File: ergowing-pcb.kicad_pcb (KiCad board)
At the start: 2 copper layers, 309.6 x 110.8 mm, 156 parts, among them J1 USB_mini_micro_B, K0:0 KEYSW, K0:1 KEYSW, K0:2 KEYSW, K0:3 KEYSW, K0:4 KEYSW, K10:0 KEYSW, K10:1 KEYSW, K10:2 KEYSW, K10:3 KEYSW, K10:4 KEYSW, K11:0 KEYSW, K11:1 KEYSW, K11:2 KEYSW, K11:3 KEYSW, K11:4 KEYSW, K12:0 KEYSW, K12:1 KEYSW, K12:2 KEYSW, K12:3 KEYSW, K12:4 KEYSW, K13:0 KEYSW, K13:1 KEYSW, K13:2 KEYSW, K13:3 KEYSW, K13:4 KEYSW, K1:0 KEYSW, K1:1 KEYSW, K1:2 KEYSW, K1:3 KEYSW, K1:4 KEYSW, K2:0 KEYSW, K2:1 KEYSW, K2:2 KEYSW, K2:3 KEYSW, K2:4 KEYSW, K3:0 KEYSW, K3:1 KEYSW, K3:2 KEYSW, K3:3 KEYSW, K3:4 KEYSW, K4:0 KEYSW, K4:1 KEYSW, K4:2 KEYSW, K4:3 KEYSW, K4:4 KEYSW, K5:0 KEYSW, K5:1 KEYSW, K5:2 KEYSW, K5:3 KEYSW, K5:4 KEYSW, K6:0 KEYSW, K6:1 KEYSW, K6:3 KEYSW, K7:0 KEYSW, K7:1 KEYSW, K7:3 KEYSW, K7:4 KEYSW, K8:0 KEYSW, K8:1 KEYSW, K8:2 KEYSW, K8:3 KEYSW, K8:4 KEYSW, K9:0 KEYSW, K9:1 KEYSW, K9:2 KEYSW, K9:3 KEYSW, K9:4 KEYSW, SW1 SW_PUSH, U1 ATMEGA32U4, X1 XTAL_GND

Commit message: Edge cuts lined up
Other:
- board size 309.6 x 110.8 mm -> 309.8 x 110.9 mm
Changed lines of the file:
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@@
     (links 522)
     (no_connects 0)
-    (area 46.80134 9.363663 355.995213 136.791998)
+    (area 42.554808 21.173406 352.858618 132.915581)
     (thickness 1.6)
-    (drawings 20)
+    (drawings 16)
     (tracks 1784)
     (zones 0)
@@
     (42 Eco1.User user)
     (43 Eco2.User user)
-    (44 Edge.Cuts user hide)
+    (44 Edge.Cuts user)
     (45 Margin user)
     (46 B.CrtYd user)
@@
   (gr_line (start 42.815024 119.692888) (end 51.430988 21.223407) (layer Eco1.User) (width 0.1))
   (gr_line (start 183.806712 132.140235) (end 42.815024 119.692888) (layer Eco1.User) (width 0.1))
-  (gr_line (start 351.218732 119.944908) (end 211.806719 132.140236) (layer Edge.Cuts) (width 0.15))
-  (gr_line (start 344.111389 22.59822) (end 352.491387 118.428217) (layer Edge.Cuts) (width 0.15))
-  (gr_line (start 203.656716 33.480237) (end 342.594697 21.325566) (angle 90) (layer Edge.Cuts) (width 0.15))
-  (gr_arc (start 342.716712 22.720234) (end 342.594697 21.325566) (angle 90) (layer Edge.Cuts) (width 0.15))
-  (gr_arc (start 351.096713 118.550241) (end 352.491387 118.428217) (angle 90) (layer Edge.Cuts) (width 0.15))
-  (gr_line (start 183.806712 132.140235) (end 44.209696 119.814906) (angle 90) (layer Edge.Cuts) (width 0.15))
-  (gr_line (start 191.756716 33.480241) (end 52.828733 21.345561) (angle 90) (layer Edge.Cuts) (width 0.15))
-  (gr_line (start 51.312043 22.618219) (end 42.937044 118.298221) (angle 90) (layer Edge.Cuts) (width 0.15))
-  (gr_arc (start 44.331715 118.420236) (end 44.209696 119.814906) (angle 90) (layer Edge.Cuts) (width 0.15))
-  (gr_arc (start 52.706714 22.740234) (end 51.312043 22.618219) (angle 90) (layer Edge.Cuts) (width 0.15))
-  (gr_line (start 191.756716 33.480241) (end 203.656716 33.480237) (angle 90) (layer Edge.Cuts) (width 0.15))
-  (gr_line (start 183.806712 132.140235) (end 211.806719 132.140236) (angle 90) (layer Edge.Cuts) (width 0.15))
+  (gr_line (start 352.618833 119.820771) (end 211.806713 132.140235) (layer Edge.Cuts) (width 0.15))
+  (gr_line (start 352.618833 119.820771) (end 343.991114 21.223471) (layer Edge.Cuts) (width 0.15))
+  (gr_line (start 203.656715 33.500237) (end 343.991114 21.223471) (angle 90) (layer Edge.Cuts) (width 0.15))
+  (gr_line (start 183.806712 132.140235) (end 42.815024 119.692888) (angle 90) (layer Edge.Cuts) (width 0.15))
+  (gr_line (start 51.430988 21.223407) (end 191.754973 33.500165) (angle 90) (layer Edge.Cuts) (width 0.15))
+  (gr_line (start 42.815024 119.692888) (end 51.430988 21.223407) (angle 90) (layer Edge.Cuts) (width 0.15))
+  (gr_line (start 191.754973 33.500165) (end 203.656715 33.500237) (angle 90) (layer Edge.Cuts) (width 0.15))
+  (gr_line (start 183.806712 132.140235) (end 211.806713 132.140235) (angle 90) (layer Edge.Cuts) (width 0.15))
   (segment (start 204.506716 100.650233) (end 204.506714 100.620234) (width 0.25) (layer B.Cu) (net 1))
   (segment (start 204.506714 100.620234) (end 202.7206 98.834118) (width 0.25) (layer B.Cu) (net 1))

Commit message: Update#1
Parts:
- moved D10:3 118.7 mm to (278.1, 216.4)
- moved D11:0 118.7 mm to (292.1, 160.2)
- moved D13:1 118.7 mm to (336.0, 178.5)
- moved D4:3 118.7 mm to (141.8, 219.6)
- moved K10:4 118.7 mm to (279.3, 230.8)
- moved K11:0 118.7 mm to (291.6, 155.8)
- moved K8:3 118.7 mm to (240.5, 218.1)
- moved C2 118.7 mm to (211.9, 223.0)
- moved D5:1 118.7 mm to (163.7, 185.1)
- moved K12:1 118.7 mm to (312.2, 176.1)
- moved K2:0 118.7 mm to (109.6, 155.8)
- moved K2:3 118.7 mm to (104.7, 212.0)
- moved K6:1 118.7 mm to (182.4, 187.1)
- moved U1 118.7 mm to (200.7, 228.2)
- moved X1 118.7 mm to (208.5, 220.1)
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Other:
- board size 309.8 x 110.9 mm -> 140.8 x 12.3 mm

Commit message: Start re-aligning keyswitches
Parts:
- moved D0:0 86.0 mm to (64.6, 245.6), turned to 0 degrees
- moved K0:0 86.0 mm to (64.6, 241.2), turned to 5 degrees
- moved K0:1 67.2 mm to (64.6, 241.2), turned to 5 degrees
- moved D0:1 67.2 mm to (64.6, 245.6), turned to 0 degrees
- moved D0:2 48.5 mm to (64.6, 245.6), turned to 0 degrees
- moved K0:2 48.5 mm to (64.6, 241.2), turned to 5 degrees
- moved D0:3 29.9 mm to (64.6, 245.6), turned to 0 degrees
- moved K0:3 29.9 mm to (64.6, 241.2), turned to 5 degrees
- moved D13:4 13.8 mm to (344.2, 221.3), turned to 10 degrees
- moved K13:4 13.6 mm to (343.5, 216.9), turned to 5 degrees
- moved D13:3 13.3 mm to (341.0, 202.8), turned to 10 degrees
- moved K13:3 13.2 mm to (340.2, 198.4), turned to 5 degrees
- moved K13:0 13.0 mm to (330.4, 142.8), turned to 5 degrees
- moved D13:2 13.0 mm to (337.8, 184.2), turned to 10 degrees
- moved D13:0 13.0 mm to (331.3, 147.2), turned to 10 degrees
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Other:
- board outline removed

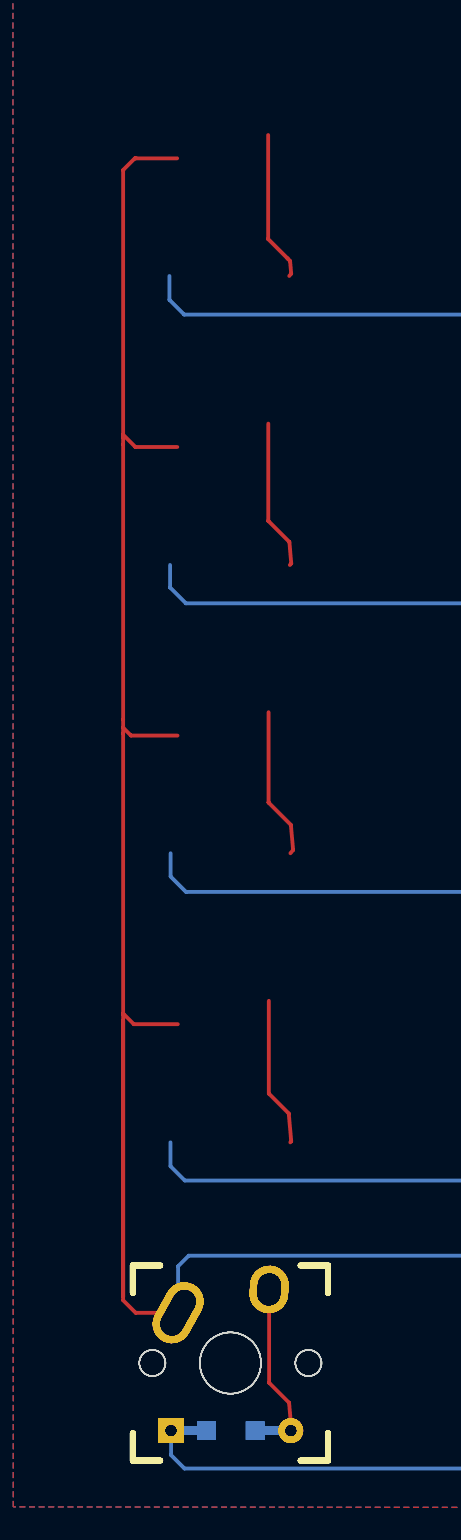
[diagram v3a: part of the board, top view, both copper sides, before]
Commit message: Col0 re-aligned *properly
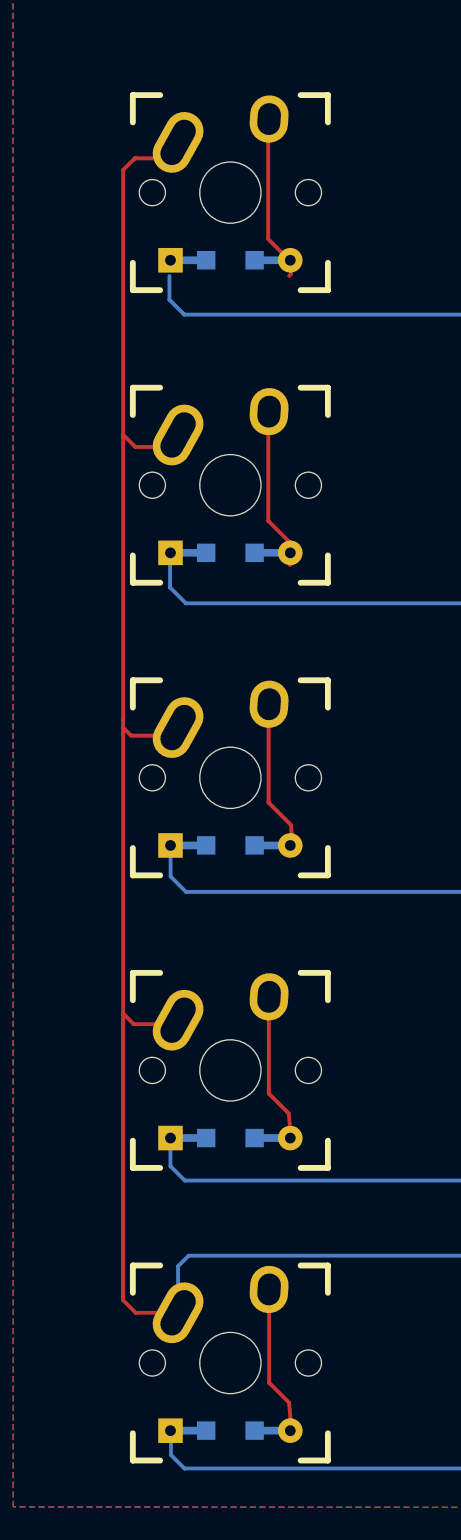
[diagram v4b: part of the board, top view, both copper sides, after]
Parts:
- moved D0:0 76.2 mm to (64.6, 169.4)
- moved K0:0 76.2 mm to (64.6, 165.0)
- moved D0:1 57.2 mm to (64.6, 188.5)
- moved K0:1 57.2 mm to (64.6, 184.1)
- moved D0:2 38.1 mm to (64.6, 207.5)
- moved K0:2 38.1 mm to (64.6, 203.1)
- moved D0:3 19.1 mm to (64.6, 226.6)
- moved K0:3 19.0 mm to (64.6, 222.2)
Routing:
- net (no net): track 0.00 -> 39.3 mm
- net row4: track 344.4 -> 318.8 mm
- net row0: track 364.4 -> 390.0 mm
- net Net-(D0:0-Pad2): track 9.82 -> 0.00 mm
- net Net-(D0:3-Pad2): track 9.78 -> 0.00 mm
- net Net-(D0:4-Pad2): track 9.75 -> 0.00 mm
- net Net-(D0:1-Pad2): track 9.81 -> 3.69 mm
- net Net-(D0:2-Pad2): track 9.86 -> 6.06 mm

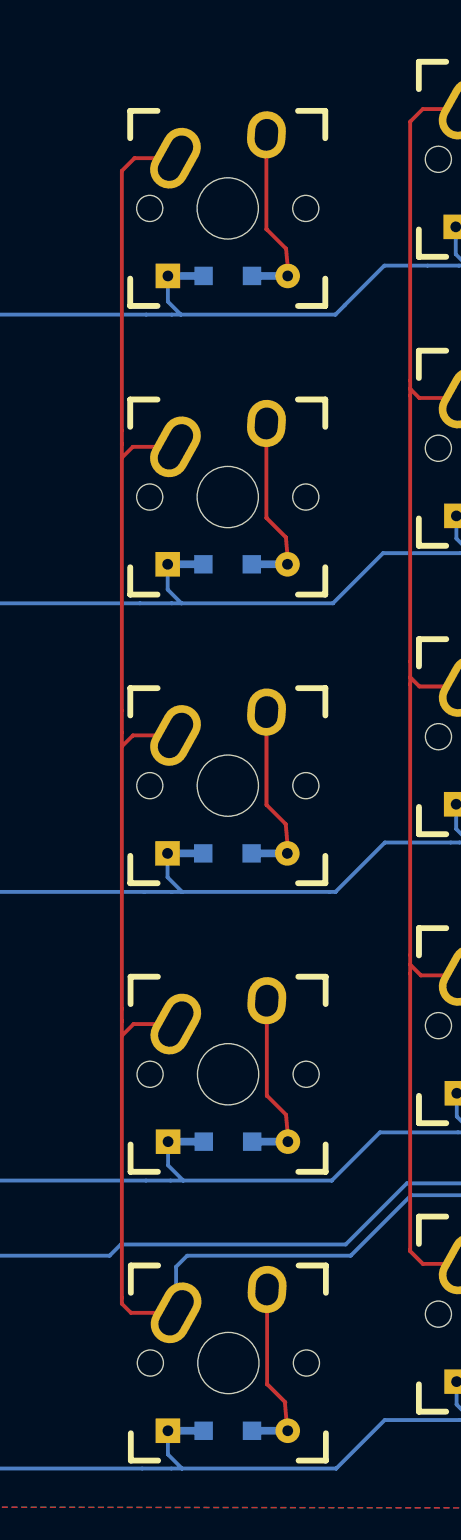
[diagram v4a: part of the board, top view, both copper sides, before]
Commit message: Col1 re-aligned
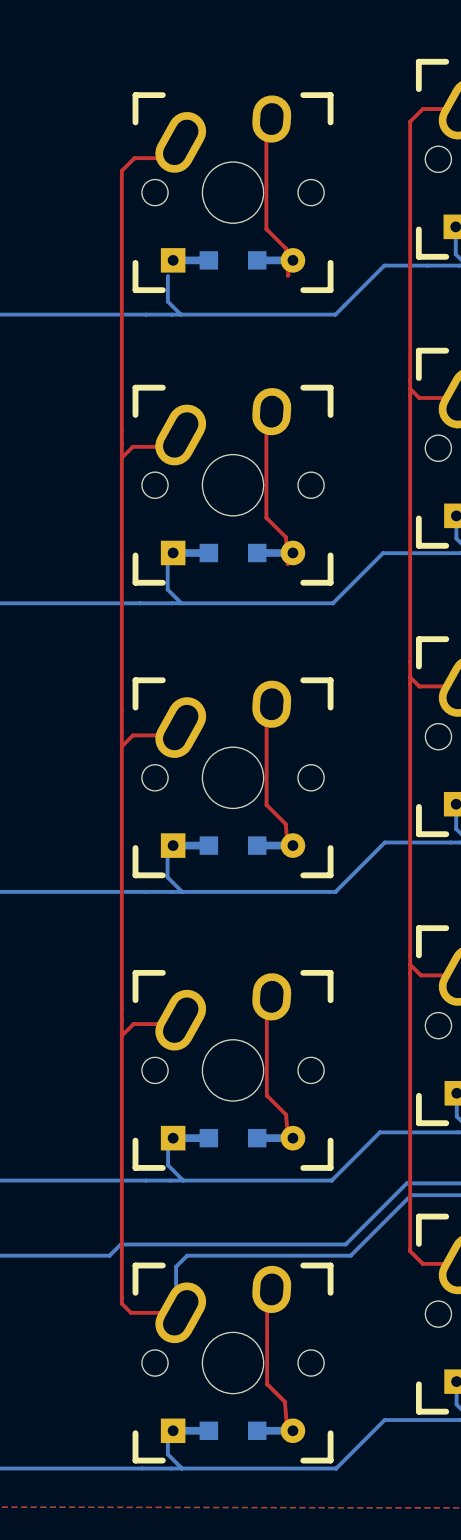
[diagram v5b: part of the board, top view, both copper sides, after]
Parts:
- moved K1:0 1.08 mm to (88.4, 165.0)
- moved D1:0 1.07 mm to (88.4, 169.4)
- moved K1:1 0.84 mm to (88.4, 184.1)
- moved D1:1 0.82 mm to (88.4, 188.5)
- moved D1:2 0.63 mm to (88.4, 207.5)
- moved K1:2 0.61 mm to (88.4, 203.1)
- moved K1:3 0.41 mm to (88.4, 222.2)
- moved D1:3 0.40 mm to (88.4, 226.6)
- moved D1:4 0.34 mm to (88.4, 245.6)
- moved K1:4 0.30 mm to (88.4, 241.2)
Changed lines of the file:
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@@
   )
   (module keyboard_parts:D_SOD123_axial (layer B.Cu)
-    (at 88.086813 170.44583)
+    (at 88.428438 169.431682)
     (attr smd)
     (fp_text reference D1:0 (at 0 -1.925) (layer B.SilkS)
@@
   )
   (module keyboard_parts:D_SOD123_axial (layer B.Cu)
-    (at 88.072898 189.21848)
+    (at 88.428438 188.481682)
     (attr smd)
     (fp_text reference D1:1 (at 0 -1.925) (layer B.SilkS)
@@
   )
   (module keyboard_parts:D_SOD123_axial (layer B.Cu)
-    (at 88.063343 208.040943)
+    (at 88.428438 207.531682)
     (attr smd)
     (fp_text reference D1:2 (at 0 -1.925) (layer B.SilkS)
@@
   )
   (module keyboard_parts:D_SOD123_axial (layer B.Cu)
-    (at 88.099248 226.809232)
+    (at 88.428438 226.581682)
     (attr smd)
     (fp_text reference D1:3 (at 0 -1.925) (layer B.SilkS)
@@
   )
   (module keyboard_parts:D_SOD123_axial (layer B.Cu)
-    (at 88.089702 245.631682)
+    (at 88.428438 245.631682)
     (attr smd)
     (fp_text reference D1:4 (at 0 -1.925) (layer B.SilkS)
@@
   )
   (module keebs:Mx_Alps_100_R-5deg (layer F.Cu)
-    (at 88.083627 166.049383 5)
+    (at 88.428438 165.020778 5)
     (descr MXALPS)
     (tags MXALPS)
@@
   )
   (module keebs:Mx_Alps_100_R-5deg (layer F.Cu)
-    (at 88.08391 184.840868 5)
+    (at 88.428438 184.070778 5)
     (descr MXALPS)
     (tags MXALPS)
@@
   )
   (module keebs:Mx_Alps_100_R-5deg (layer F.Cu)
-    (at 88.089171 203.631911 5)
+    (at 88.428438 203.120778 5)
     (descr MXALPS)
     (tags MXALPS)
@@
   )
   (module keebs:Mx_Alps_100_R-5deg (layer F.Cu)
-    (at 88.106897 222.421863 5)
+    (at 88.428438 222.170778 5)
     (descr MXALPS)
     (tags MXALPS)
@@
   )
   (module keebs:Mx_Alps_100_R-5deg (layer F.Cu)
-    (at 88.125492 241.221789 5)
+    (at 88.428438 241.220778 5)
     (descr MXALPS)
     (tags MXALPS)

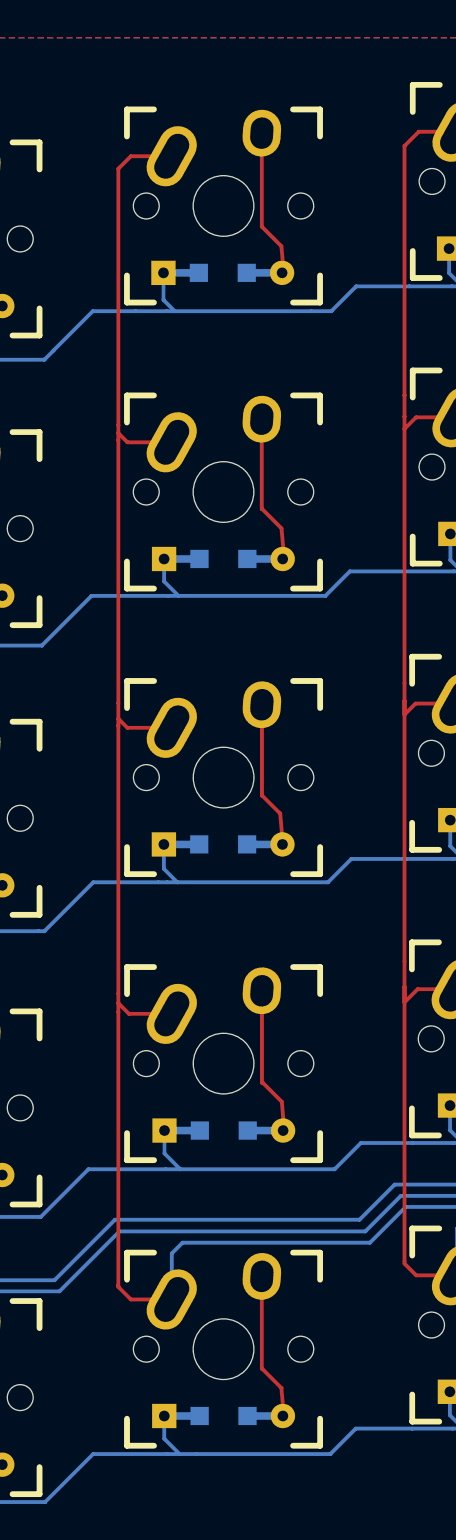
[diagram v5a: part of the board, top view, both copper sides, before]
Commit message: Col2 re-aligned
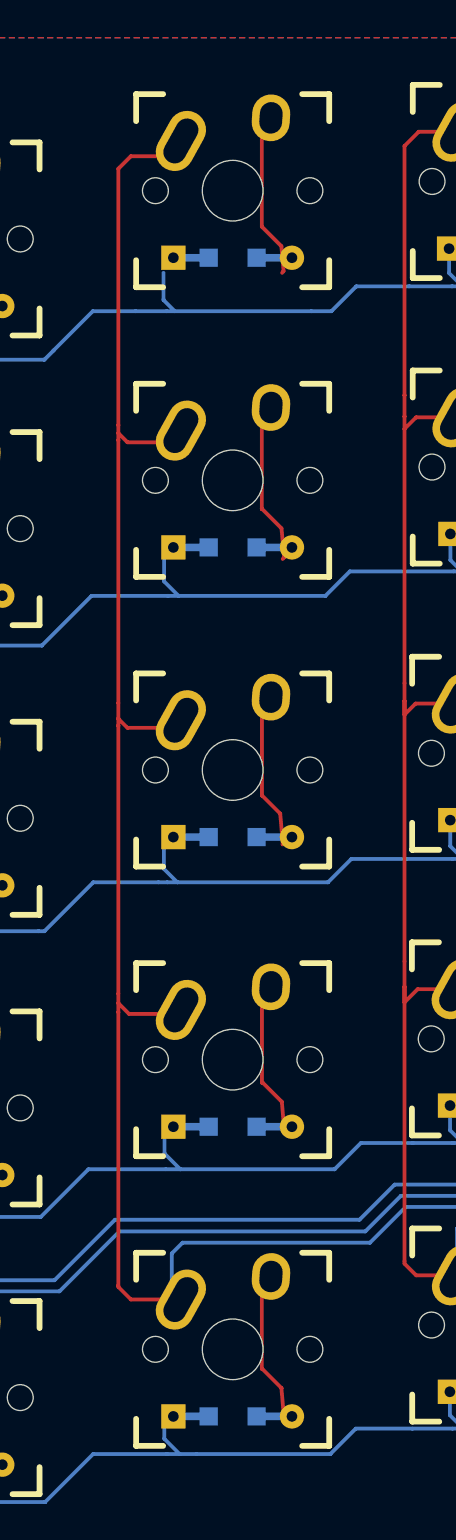
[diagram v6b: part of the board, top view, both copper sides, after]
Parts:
- moved D2:0 1.19 mm to (107.5, 166.3)
- moved K2:0 1.17 mm to (107.5, 161.8)
- moved K2:1 0.98 mm to (107.5, 180.9)
- moved D2:1 0.97 mm to (107.5, 185.3)
- moved D2:2 0.79 mm to (107.5, 204.4)
- moved K2:2 0.78 mm to (107.5, 199.9)
- moved K2:3 0.65 mm to (107.5, 219.0)
- moved D2:3 0.63 mm to (107.5, 223.4)
- moved K2:4 0.60 mm to (107.5, 238.0)
- moved D2:4 0.60 mm to (107.5, 242.5)
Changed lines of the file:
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@@
   )
   (module keyboard_parts:D_SOD123_axial (layer B.Cu)
-    (at 106.82961 167.25013)
+    (at 107.478438 166.256682)
     (attr smd)
     (fp_text reference D2:0 (at 0 -1.925) (layer B.SilkS)
@@
   )
   (module keyboard_parts:D_SOD123_axial (layer B.Cu)
-    (at 106.86987 186.068232)
+    (at 107.478438 185.306682)
     (attr smd)
     (fp_text reference D2:1 (at 0 -1.925) (layer B.SilkS)
@@
   )
   (module keyboard_parts:D_SOD123_axial (layer B.Cu)
-    (at 106.855957 204.840883)
+    (at 107.478438 204.356682)
     (attr smd)
     (fp_text reference D2:2 (at 0 -1.925) (layer B.SilkS)
@@
   )
   (module keyboard_parts:D_SOD123_axial (layer B.Cu)
-    (at 106.896219 223.658979)
+    (at 107.478438 223.406682)
     (attr smd)
     (fp_text reference D2:3 (at 0 -1.925) (layer B.SilkS)
@@
   )
   (module keyboard_parts:D_SOD123_axial (layer B.Cu)
-    (at 106.882312 242.431625)
+    (at 107.478438 242.456682)
     (attr smd)
     (fp_text reference D2:4 (at 0 -1.925) (layer B.SilkS)
@@
   )
   (module keebs:Mx_Alps_100_R-5deg (layer F.Cu)
-    (at 106.876449 162.851818 5)
+    (at 107.478438 161.845778 5)
     (descr MXALPS)
     (tags MXALPS)
@@
   )
   (module keebs:Mx_Alps_100_R-5deg (layer F.Cu)
-    (at 106.87599 181.663439 5)
+    (at 107.478438 180.895778 5)
     (descr MXALPS)
     (tags MXALPS)
@@
   )
   (module keebs:Mx_Alps_100_R-5deg (layer F.Cu)
-    (at 106.882875 200.444304 5)
+    (at 107.478438 199.945778 5)
     (descr MXALPS)
     (tags MXALPS)
@@
   )
   (module keebs:Mx_Alps_100_R-5deg (layer F.Cu)
-    (at 106.882411 219.255933 5)
+    (at 107.478438 218.995778 5)
     (descr MXALPS)
     (tags MXALPS)
@@
   )
   (module keebs:Mx_Alps_100_R-5deg (layer F.Cu)
-    (at 106.879341 238.037669 5)
+    (at 107.478438 238.045778 5)
     (descr MXALPS)
     (tags MXALPS)
